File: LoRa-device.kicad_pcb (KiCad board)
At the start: 4 copper layers, 86.4 x 50.8 mm, 156 parts, among them J1 Micro_SD_Card_Det1, J3 Conn_01x04_Pin, J4 Conn_01x14_Pin, J6 Conn_01x04_Pin, J8 U.FL, P1 1_25T-1-2A, SW1 EVQPUC02K, SW2 EVQPUC02K, U1 ESP32-S3, U10 TPS2116DRL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

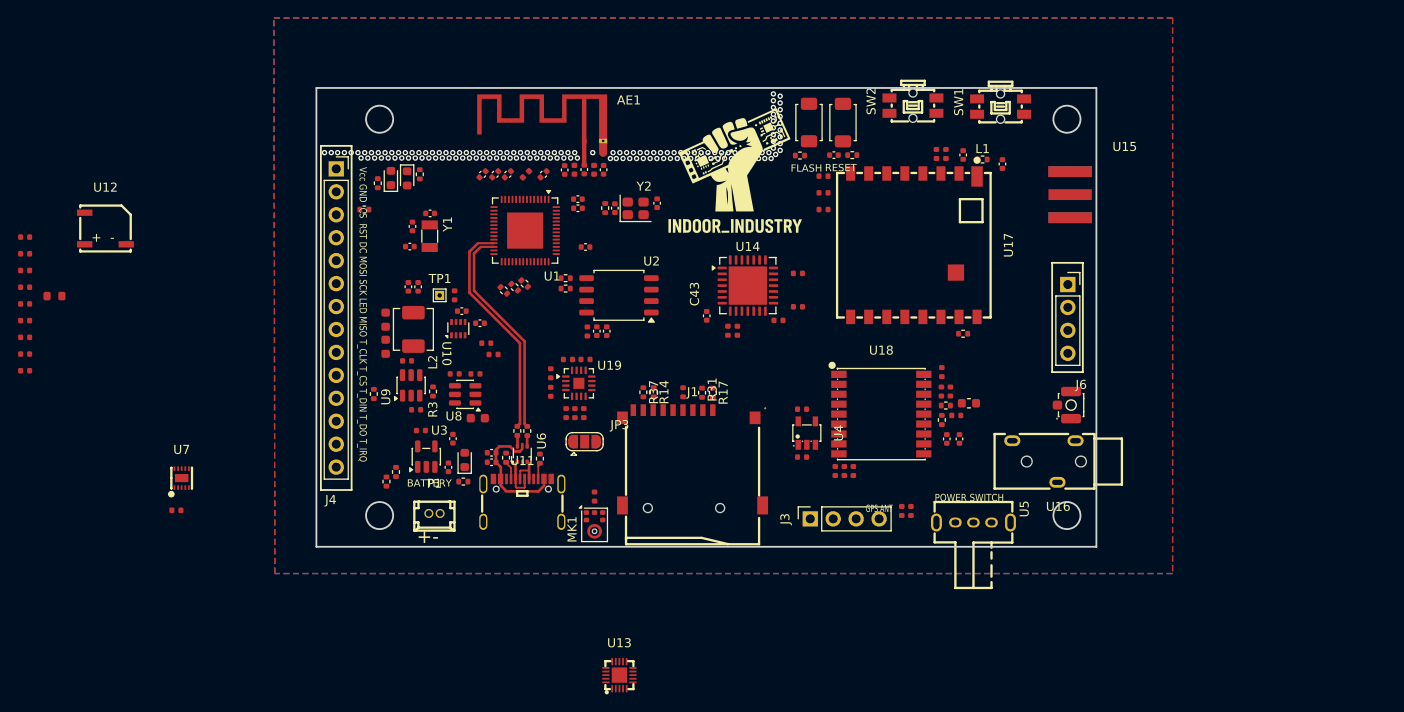
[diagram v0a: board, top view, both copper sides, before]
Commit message: Added buttons to case, rehauled power supply.
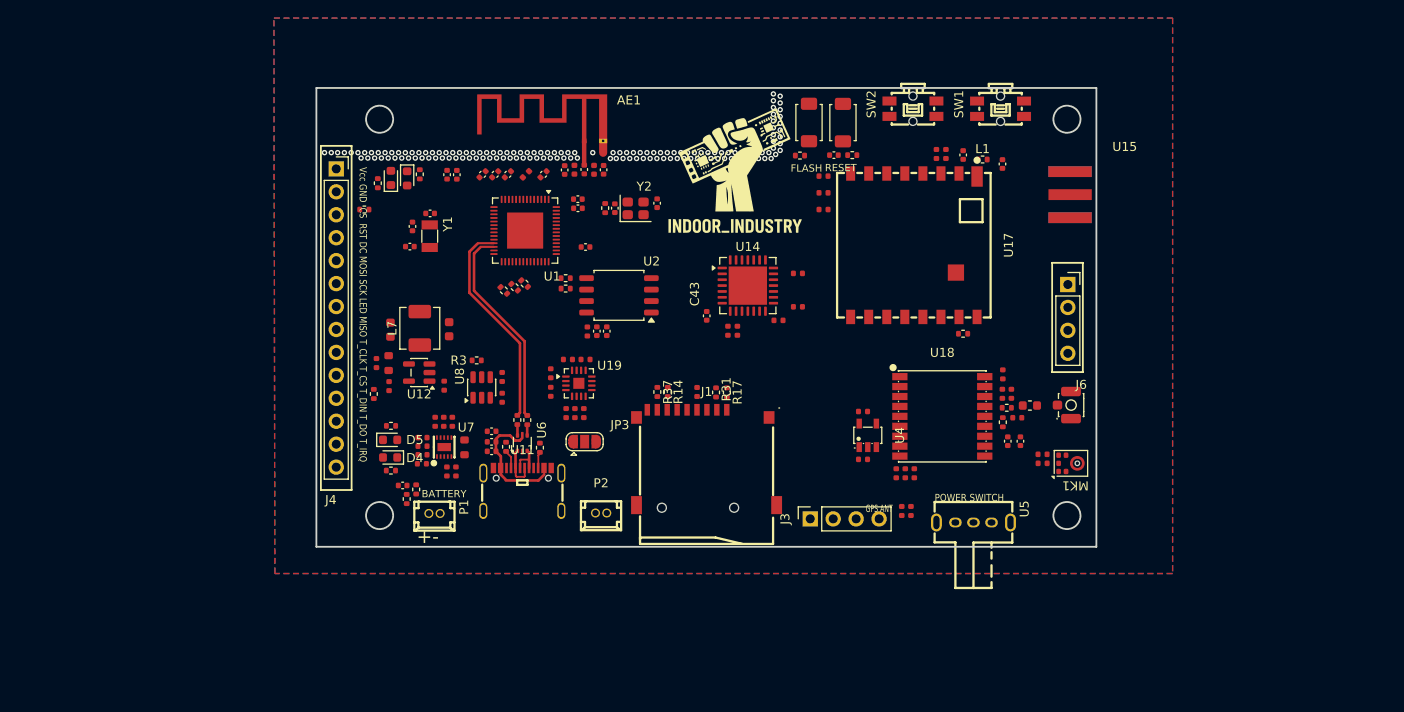
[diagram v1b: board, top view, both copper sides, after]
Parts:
- removed C1: 1uF, Capacitor_SMD:C_0402_1005Metric
- removed C12, C21, C50: 22uF, PCM_JLCPCB:C_0603
- removed C2: 10uF, Capacitor_SMD:C_0402_1005Metric
- removed C5: 10uF, PCM_JLCPCB:C_0402
- removed C9: 100nF, PCM_JLCPCB:C_0402
- removed D1: LED, LED_SMD:LED_0603_1608Metric
- removed L2: 4.7uH 3V, Inductor_SMD:L_Sunlord_MWSA0402S
- removed R15: 1K, Resistor_SMD:R_0402_1005Metric
- removed R20: 4.7kΩ, PCM_JLCPCB:R_0402
- removed R32: 100kΩ, PCM_JLCPCB:R_0402
- removed R33: 8.2kΩ, PCM_JLCPCB:R_0402
- removed R6: 22kΩ, PCM_JLCPCB:R_0402
- removed TP1: TestPoint, TestPoint:TestPoint_THTPad_1.0x1.0mm_Drill0.5mm
- removed U10: TPS2116DRL, Package_TO_SOT_SMD:SOT-583-8
- removed U13: ES8311, LoRa_library:WQFN-20_L3.0-W3.0-P0.40-BL-EP1.7
- removed U16: Black_headphone_jack, LoRa_library:AUDIO-TH_320B
- removed U3: TP4055, Package_TO_SOT_SMD:SOT-23-5
- removed U9: AP63203WU, Package_TO_SOT_SMD:TSOT-23-6
- added C54: 4.7uF, PCM_JLCPCB:C_0402, F.Cu at (116.0, 106.8)
- added C55: 10uF, PCM_JLCPCB:C_0603, F.Cu at (116.6, 100.5)
- added C56: 22uF, PCM_JLCPCB:C_0603, F.Cu at (110.1, 100.6)
- added C57: 6.8pF, PCM_JLCPCB:C_0402, F.Cu at (108.5, 104.3)
- added D4: LED, LED_SMD:LED_0603_1608Metric, F.Cu at (110.1, 114.8)
- added D5: LED, LED_SMD:LED_0603_1608Metric, F.Cu at (110.1, 112.8)
- added L7: 4.7uH 3V, Inductor_SMD:L_Sunlord_MWSA0402S, F.Cu at (113.3, 100.5)
- added P2: 1_25T-1-2A, LoRa_library:CONN-TH_1.25T-1-2A, F.Cu at (133.4, 120.9)
- added R54: 1K, Resistor_SMD:R_0402_1005Metric, F.Cu at (110.2, 116.2)
- added R55: 1K, Resistor_SMD:R_0402_1005Metric, F.Cu at (110.2, 111.2)
- added R56: 150kΩ, PCM_JLCPCB:R_0402, F.Cu at (110.0, 106.8)
- added R57: 680kΩ, PCM_JLCPCB:R_0603, F.Cu at (109.9, 104.3)
- U12: value MLT-5020 -> TLV62569DBV; footprint LoRa_library:BUZ-SMD_L5.0-W5.5-P4.60 -> Package_TO_SOT_SMD:SOT-23-5
- moved R1 96.1 mm to (182.3, 114.4), turned to 180 degrees
- moved MK1 53.2 mm to (185.4, 115.4), turned to 90 degrees
- moved R41 51.2 mm to (117.4, 116.3), turned to -90 degrees
- moved R43 49.7 mm to (182.3, 115.4), turned to 180 degrees
- moved C42 49.7 mm to (113.7, 113.5), turned to 180 degrees
- moved R49 48.6 mm to (117.0, 110.8), turned to 90 degrees
- moved C52 48.5 mm to (113.7, 114.4), turned to 180 degrees
- moved C51 48.5 mm to (113.7, 112.5), turned to 180 degrees
- moved R52 48.5 mm to (116.4, 116.3), turned to 90 degrees
- moved R51 48.4 mm to (118.3, 113.6), turned to -90 degrees
- moved C53 48.1 mm to (113.6, 115.4), turned to 180 degrees
- moved R50 47.3 mm to (116.0, 110.8), turned to 90 degrees
- moved R53 45.8 mm to (115.1, 110.8), turned to -90 degrees
- moved U12 38.2 mm to (113.3, 105.3), turned to 180 degrees
- moved U7 29.3 mm to (116.0, 113.6)
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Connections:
- R52 pad 2: Net-(U7-STAT2) -> GPB5
- R53 pad 2: Net-(U7-STAT1) -> GPA1
- U12 pad 1: unconnected-(U12-+-Pad1) -> VSYS_SW
- U12 pad 2: unconnected-(U12---Pad2) -> GND
- U12 pad 3: unconnected-(U12-NC-Pad3) -> Net-(U12-SW)
- U14 pad 18: unconnected-(U14-GPA1-Pad18) -> GPA1
- U14 pad 2: unconnected-(U14-GPB5-Pad2) -> GPB5
- U7 pad 3: Net-(U7-STAT2) -> GPB5
- U7 pad 9: Net-(U7-STAT1) -> GPA1
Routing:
- net USB_D+: track 24.0 -> 22.8 mm
- net USB_D-: track 24.8 -> 23.6 mm

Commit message: Almost ready for routing, major fixes, case ready.
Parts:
- removed C34: 1uF, PCM_JLCPCB:C_0402
- removed C51: 2.2uF, PCM_JLCPCB:C_0402
- removed C52: 10uF, PCM_JLCPCB:C_0402
- removed R57: 680kΩ, PCM_JLCPCB:R_0603
- added C1: 2.2uF, PCM_JLCPCB:C_0603, F.Cu at (113.7, 111.3)
- added C2: 10uF, PCM_JLCPCB:C_0603, F.Cu at (116.0, 116.8)
- added C5: 4.7uF, PCM_JLCPCB:C_0402, F.Cu at (162.5, 108.6)
- added C9: 100nF, PCM_JLCPCB:C_0402, F.Cu at (162.5, 109.7)
- added R32: 510Ω, PCM_JLCPCB:R_0402, F.Cu at (116.0, 110.8)
- added R33: 100kΩ, PCM_JLCPCB:R_0402, F.Cu at (112.8, 108.5)
- R50: value 330Ω -> 300kΩ; footprint PCM_JLCPCB:R_0402 -> PCM_JLCPCB:R_0603
- R56: footprint PCM_JLCPCB:R_0402 -> PCM_JLCPCB:R_0603
- moved R50 5.50 mm to (110.8, 109.2), turned to 180 degrees
- moved C36 3.07 mm to (174.1, 83.0)
- moved DNP2 3.07 mm to (176.0, 83.1)
- moved L1 3.07 mm to (178.1, 83.6)
- moved R10 3.07 mm to (175.9, 102.9)
- moved R44 3.07 mm to (160.5, 89.2)
- moved R46 3.07 mm to (160.5, 85.5)
- moved C7 3.07 mm to (173.0, 83.0)
- moved DNP4 3.07 mm to (180.3, 84.1)
- moved R45 3.07 mm to (160.5, 87.3)
- moved U17 3.07 mm to (170.5, 93.1)
- moved R56 1.13 mm to (110.8, 107.7), turned to 0 degrees
- moved R41 0.85 mm to (118.2, 116.3)
- moved R52 0.85 mm to (117.2, 116.3)
- moved C44 0.81 mm to (166.7, 121.5)
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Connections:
- D3 pad 2: GPA5 -> GPA7
- R50 pad 1: Net-(U7-ISET) -> VDD_CPU
- R50 pad 2: GND -> Net-(R50-Pad2)
- R56 pad 1: Net-(U12-FB) -> Net-(R50-Pad2)
- R56 pad 2: GND -> Net-(U12-FB)
- SW1 pad 3: GPA7 -> GPA5
- SW2 pad 3: GPB7 -> GPB2
- U14 pad 27: LORA_RF_EN -> GPB2
- U14 pad 4: GPB7 -> LORA_RF_EN
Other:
- outline, holes or cut-outs redrawn
- board text added: "AUDIO OUT"

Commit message: Case prototype ready. Added thermal pads.
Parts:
- removed C57: 6.8pF, PCM_JLCPCB:C_0402
- removed R24, R42: 330Ω, PCM_JLCPCB:R_0402
- added R15: 33Ω, PCM_JLCPCB:R_0402, F.Cu at (158.9, 118.8)
- added R20: 33Ω, PCM_JLCPCB:R_0402, F.Cu at (156.5, 118.8)
- added R6: 330Ω, PCM_JLCPCB:R_0402, F.Cu at (130.8, 91.9)
- moved DNP1 4.25 mm to (127.5, 86.7), turned to -45 degrees
- moved C14 3.83 mm to (132.9, 86.7), turned to -45 degrees
- moved R30 3.62 mm to (125.0, 99.0)
- moved L6 3.21 mm to (128.3, 85.2), turned to 45 degrees
- moved R29 3.06 mm to (125.8, 98.3)
- moved L5 2.61 mm to (131.5, 85.2), turned to 135 degrees
- moved C39 2.60 mm to (129.4, 89.3)
- moved C40 2.60 mm to (129.3, 88.3)
- moved R28 2.56 mm to (126.5, 97.5)
- moved C33 2.29 mm to (138.8, 88.7)
- moved R23 2.29 mm to (133.0, 89.3)
- moved Y2 2.29 mm to (136.4, 89.3)
- moved C38 2.29 mm to (111.7, 91.3)
- moved U1 2.29 mm to (124.2, 91.8)
- moved Y1 2.29 mm to (113.6, 92.4)
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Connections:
- J3 pad 1: MTDO/IO40/I2C_SCK -> Net-(J3-Pin_1)
- J3 pad 2: MTMS/IO42/I2C_SDA -> Net-(J3-Pin_2)
- R47 pad 2: MTMS/IO42/I2C_SDA -> Net-(J3-Pin_2)
- R48 pad 2: MTDO/IO40/I2C_SCK -> Net-(J3-Pin_1)
- U1 pad 45: Net-(U1-MTDO) -> MTDO/IO40/I2C_SCK
- U1 pad 48: Net-(U1-MTMS) -> MTMS/IO42/I2C_SDA
- U1 pad 49: GPS_RXD -> Net-(U1-U0TXD)
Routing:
- net Net-(AE1-FEED): track 2.63 -> 8.26 mm
- net Net-(U1-LNA_IN): track 0.00 -> 3.30 mm
- net USB_D-: track 23.6 -> 22.9 mm
- net USB_D+: track 22.8 -> 22.2 mm
- added copper zone on In2.Cu, net GND
- removed copper zone on In2.Cu, net VDD_CPU

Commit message: Ready for routing!
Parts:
- removed DNP1: ~, Capacitor_SMD:C_0402_1005Metric
- removed L4: 68nH,300mA, PCM_JLCPCB:L_0603
- added C12: 1.4pF, Capacitor_SMD:C_0402_1005Metric, F.Cu at (126.7, 85.9)
- added JP1: Jumper_2_Open, Jumper:SolderJumper-2_P1.3mm_Open_RoundedPad1.0x1.5mm, F.Cu at (109.5, 95.8)
- added L2: 68nH, Inductor_SMD:L_0402_1005Metric, F.Cu at (182.2, 107.8)
- C31: value 15pF -> 1.4pF
- L6: value 4.7nH -> 2.7nH
- moved J4 33.0 mm to (103.9, 115.8), turned to 180 degrees
- moved R44 7.63 mm to (165.4, 83.3)
- moved R45 4.94 mm to (163.4, 83.3)
- moved G*** 4.79 mm to (147.1, 89.0)
- moved R47 4.05 mm to (151.1, 103.8)
- moved U14 4.05 mm to (152.3, 98.8)
- moved C43 4.05 mm to (147.7, 102.2)
- moved R4 4.05 mm to (155.7, 102.7)
- moved R48 4.05 mm to (150.1, 103.8)
- moved DNP2 2.82 mm to (178.3, 84.6)
- moved C27 2.70 mm to (182.1, 111.2)
- moved L1 2.38 mm to (180.0, 85.0)
- moved DNP7 2.33 mm to (180.6, 110.7), turned to 90 degrees
- moved R46 2.29 mm to (161.3, 83.3)
- moved DNP4 1.93 mm to (181.7, 85.5)
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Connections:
- J1 pad 3: MOSIA -> MOSIB
- J1 pad 5: SCKA -> SCKB
- J1 pad 7: MISOA -> MISOB
- J4 pad 10: SCKB -> SCKA
- J4 pad 12: MOSIB -> MOSIA
- J4 pad 13: MISOB -> MISOA
- J4 pad 9: MISOB -> Net-(J4-Pin_9)
- R14 pad 2: MISOA -> MISOB
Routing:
- net USB_D-: track 22.9 -> 0.00 mm
- net USB_D+: track 22.2 -> 0.00 mm
- net +5V: track 13.5 -> 0.31 mm
- net Net-(AE1-FEED): track 8.26 -> 0.00 mm
- net Net-(U11-DP1): track 4.87 -> 0.00 mm
- net Net-(U11-DN1): track 4.87 -> 0.00 mm
- net Net-(U1-LNA_IN): track 3.30 -> 0.08 mm
- net Net-(U11-CC1): track 1.93 -> 0.00 mm
- net Net-(U11-CC2): track 1.76 -> 0.00 mm
- net Net-(R2-Pad1): track 1.20 -> 0.00 mm
- net Net-(R18-Pad1): track 1.19 -> 0.00 mm
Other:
- board text added: "SCK SDA GND 3V3"
- board text added: "T_IRQ T_DO T_DIN T_CS T_CLK MISO LED SCK MOSI DC RST CS GND VCC"
- board text removed: "Vcc GND CS RST DC MOSI SCK LED MISO T_CLK T_CS T_DIN T_DO T_IRQ"

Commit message: Minor layout changes
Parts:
- moved R13 22.7 mm to (108.1, 110.0), turned to -90 degrees
- moved R11 17.3 mm to (108.2, 90.4)
- moved R30 5.74 mm to (129.6, 96.0)
- moved C33 5.74 mm to (143.4, 85.6)
- moved C39 5.74 mm to (134.0, 86.2)
- moved C49 5.74 mm to (138.0, 98.6)
- moved R23 5.74 mm to (137.7, 86.2)
- moved R26 5.74 mm to (135.6, 92.7)
- moved R27 5.74 mm to (135.6, 93.8)
- moved R6 5.74 mm to (135.5, 88.8)
- moved U2 5.74 mm to (141.5, 94.6)
- moved Y1 5.74 mm to (118.3, 89.3)
- moved Y2 5.74 mm to (141.1, 86.2)
- moved C10 5.74 mm to (118.3, 86.8)
- moved C37 5.74 mm to (116.1, 90.4)
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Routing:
- net GND: track 1.32 -> 0.00 mm, vias 140 -> 142

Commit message: Routing started
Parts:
- removed JP1: Jumper_2_Open, Jumper:SolderJumper-2_P1.3mm_Open_RoundedPad1.0x1.5mm
- added H1: MountingHole, MountingHole:MountingHole_3mm, F.Cu at (184.9, 121.3)
- added H2: MountingHole, MountingHole:MountingHole_3mm, F.Cu at (108.9, 77.3)
- added H3: MountingHole, MountingHole:MountingHole_3mm, F.Cu at (184.9, 77.3)
- added H4: MountingHole, MountingHole:MountingHole_3mm, F.Cu at (108.9, 121.3)
- added R24: 0R, Resistor_SMD:R_0402_1005Metric, F.Cu at (108.3, 91.6)
- moved G*** 64.4 mm to (212.9, 97.0)
- moved D2 33.3 mm to (142.7, 91.0)
- moved R25 33.3 mm to (145.9, 90.6)
- moved D3 33.3 mm to (144.5, 91.1)
- moved R16 33.3 mm to (141.3, 91.6)
- moved R39 18.2 mm to (123.8, 83.8)
- moved R40 18.2 mm to (121.9, 83.8)
- moved R47 14.9 mm to (160.1, 117.3), turned to -90 degrees
- moved R48 14.3 mm to (157.6, 117.4), turned to -90 degrees
- moved C32 11.3 mm to (129.3, 101.5), turned to 180 degrees
- moved U2 11.3 mm to (133.3, 102.2), turned to 90 degrees
- moved R41 10.5 mm to (110.9, 108.8), turned to 90 degrees
- moved C13 9.94 mm to (129.3, 100.4), turned to 180 degrees
- moved R38 9.58 mm to (130.6, 113.0)
- moved D4 9.53 mm to (104.0, 122.1)
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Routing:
- net VDD_CPU: track 0.00 -> 252.8 mm, vias 0 -> 36
- net MOSIB: track 0.00 -> 66.4 mm, vias 0 -> 2
- net Net-(U8-~{ON}): track 0.00 -> 62.3 mm, vias 0 -> 1
- net SCKB: track 0.00 -> 61.6 mm, vias 0 -> 2
- net MISOB: track 0.00 -> 51.9 mm, vias 0 -> 2
- net TOUCH_IRQ: track 0.00 -> 49.2 mm, vias 0 -> 1
- net MOSIA: track 0.00 -> 47.6 mm, vias 0 -> 2
- net GPS_TXD: track 0.00 -> 41.7 mm
- net SCKA: track 0.00 -> 41.5 mm, vias 0 -> 2
- net GPS_RXD: track 0.00 -> 39.9 mm
- net GPA5: track 0.00 -> 36.6 mm, vias 0 -> 2
- net EN: track 0.00 -> 35.0 mm, vias 0 -> 2
- net GPB2: track 0.00 -> 31.8 mm, vias 0 -> 2
- net IO0: track 0.00 -> 30.9 mm, vias 0 -> 2
- net SCREEN_LED: track 0.00 -> 29.0 mm, vias 0 -> 1
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- added copper zone on F.Cu, net VDD_CPU
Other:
- outline, holes or cut-outs redrawn

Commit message: More routing, modifying case buttons and locking
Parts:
- moved G*** 61.3 mm to (152.3, 87.5)
- moved D2 24.1 mm to (119.4, 97.2)
- moved R16 24.1 mm to (118.0, 97.7), turned to -90 degrees
- moved R6 6.15 mm to (137.8, 93.8), turned to -45 degrees
- moved D3 3.92 mm to (140.7, 92.0)
- moved R25 3.92 mm to (142.1, 91.5)
- moved C1 2.84 mm to (117.3, 112.4)
- moved C2 2.60 mm to (117.5, 108.9), turned to 90 degrees
- moved Y1 2.16 mm to (116.5, 89.6)
- moved C37 2.16 mm to (114.7, 90.7)
- moved C38 2.16 mm to (114.7, 88.5)
- moved C42 1.88 mm to (116.8, 113.5), turned to 0 degrees
- moved C11 1.54 mm to (135.4, 91.6), turned to -45 degrees
- moved R20 1.41 mm to (155.1, 117.3)
- moved R48 1.41 mm to (156.2, 117.3)
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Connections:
- D3 pad 2: GPA7 -> GPB7
- J1 pad 2: SD_CS -> SPICLK_N/IO48/SD_CS
- R10 pad 2: SPICLK_N/IO48/LORA_CS -> LORA_CS
- R31 pad 2: SD_CS -> SPICLK_N/IO48/SD_CS
- U1 pad 10: SCREEN_DC -> LORA_IO1
- U1 pad 23: SD_CS -> SCREEN_DC
- U1 pad 24: LORA_IO1 -> SCREEN_CS
- U1 pad 36: SPICLK_N/IO48/LORA_CS -> SPICLK_N/IO48/SD_CS
- U1 pad 7: SCREEN_CS -> LORA_CS
- U14 pad 17: LORA_RST -> GPS_WKUP
- U14 pad 21: GPS_WKUP -> LORA_RST
- U14 pad 24: GPA7 -> LORA_RF_EN
- U14 pad 25: LORA_IO2 -> LORA_IO3
- U14 pad 26: LORA_IO3 -> LORA_IO2
- U14 pad 4: LORA_RF_EN -> GPB7
- U17 pad 15: SPICLK_N/IO48/LORA_CS -> LORA_CS
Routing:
- net VDD_CPU: track 252.8 -> 380.3 mm, vias 36 -> 46
- net IO8: track 0.00 -> 80.1 mm, vias 0 -> 2
- net MISOA: track 0.00 -> 78.8 mm, vias 0 -> 3
- net GPA1: track 1.69 -> 80.1 mm, vias 0 -> 2
- net SCREEN_RST: track 0.00 -> 67.8 mm, vias 0 -> 1
- net GPB5: track 7.84 -> 70.7 mm, vias 2 -> 4
- net LORA_CS: track 0.00 -> 59.6 mm, vias 0 -> 2
- net VBAT: track 10.3 -> 69.2 mm, vias 0 -> 5
- net IO4: track 0.00 -> 58.4 mm, vias 0 -> 2
- net IO1: track 0.00 -> 56.2 mm, vias 0 -> 2
- net GPA6: track 0.00 -> 53.1 mm, vias 0 -> 2
- net LORA_BUSY: track 0.00 -> 49.0 mm, vias 0 -> 2
- net LORA_IO1: track 0.00 -> 41.3 mm, vias 0 -> 2
- net IO10: track 0.00 -> 40.4 mm, vias 0 -> 2
- net SCKA: track 41.5 -> 81.2 mm, vias 2 -> 4
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- added copper zone on F.Cu, net VBAT
- added copper zone on In2.Cu, net VDD_CPU

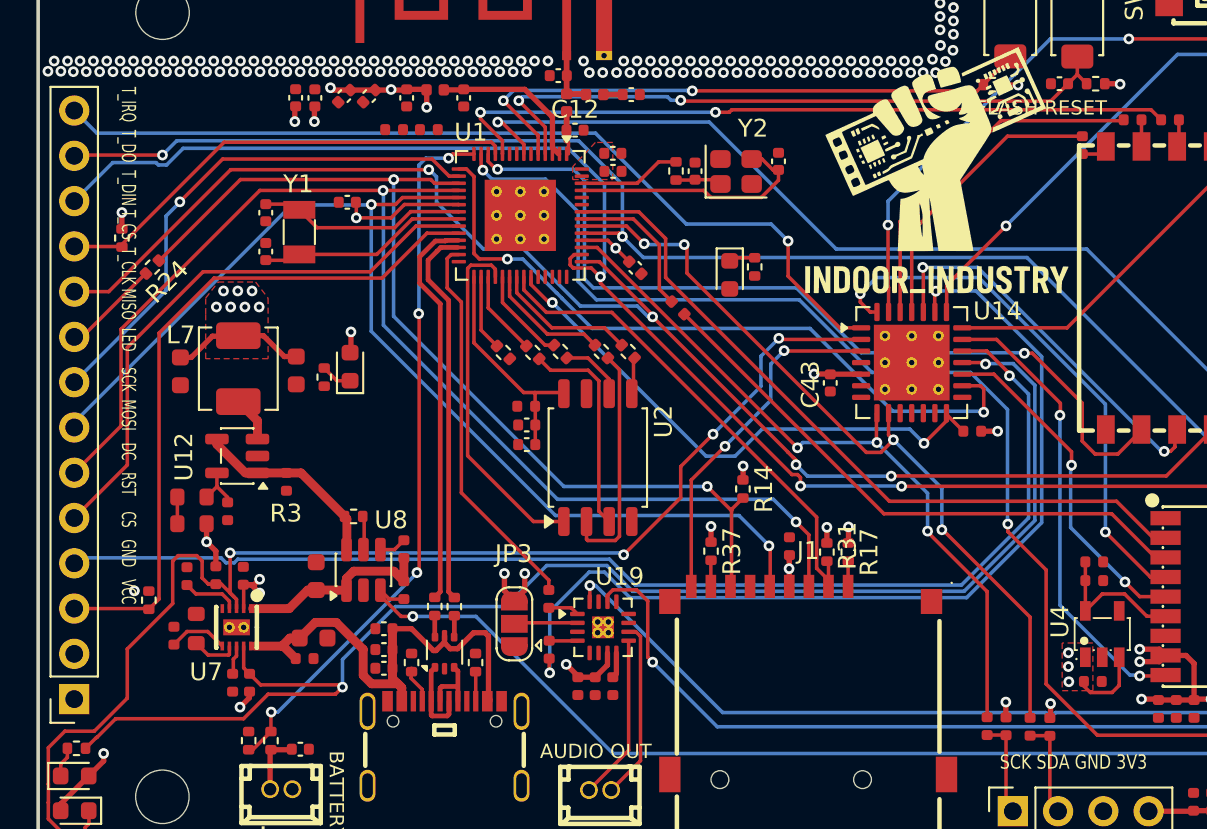
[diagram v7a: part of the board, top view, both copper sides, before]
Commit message: Modified case and progressed routing
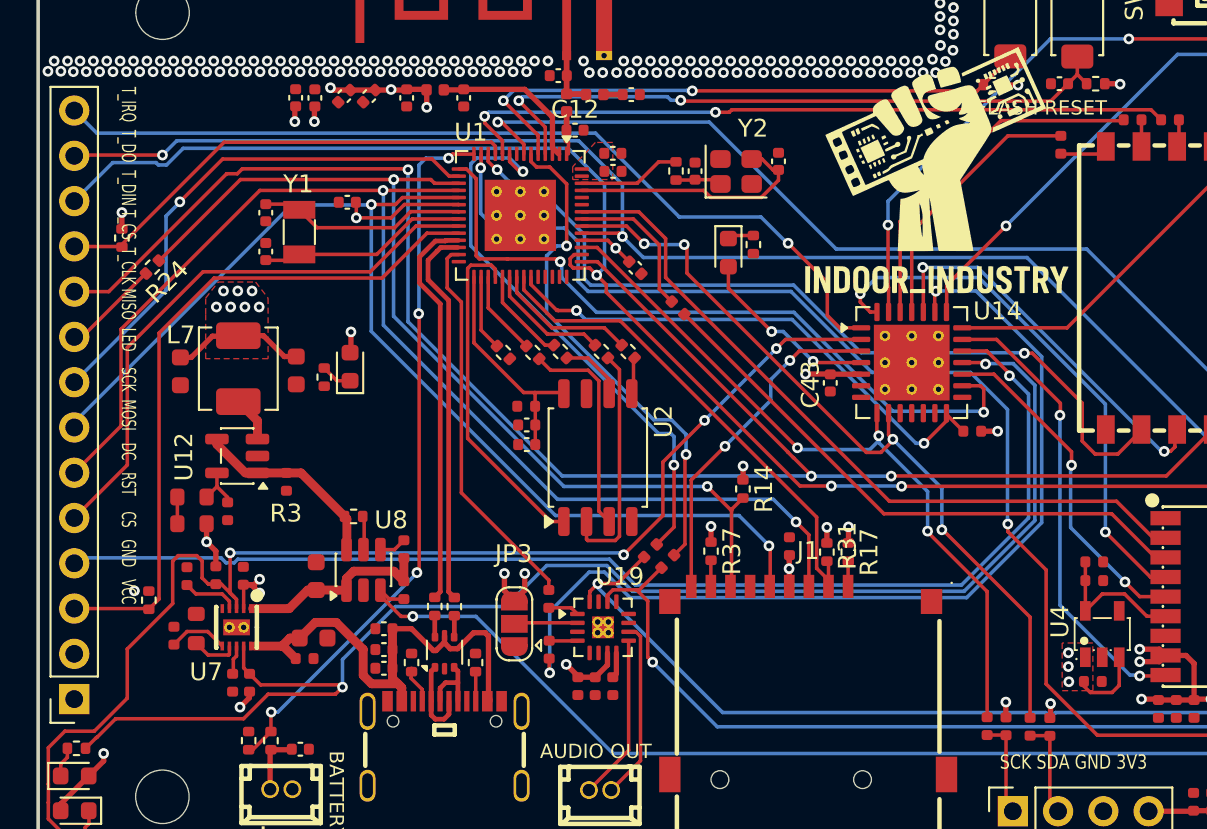
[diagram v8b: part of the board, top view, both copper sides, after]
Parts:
- moved R39 27.7 mm to (137.2, 108.1), turned to 45 degrees
- moved R40 27.7 mm to (136.2, 107.5), turned to 45 degrees
- moved D3 1.25 mm to (140.6, 90.8)
- moved R25 1.25 mm to (142.0, 90.3)
- moved R46 1.21 mm to (159.3, 84.7)
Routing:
- net Net-(U1-GPIO4): track 0.00 -> 31.7 mm, vias 0 -> 2
- net Net-(U1-GPIO1): track 0.00 -> 28.7 mm, vias 0 -> 2
- net SCKA: track 81.2 -> 97.8 mm, vias 4 -> 3
- net GPB7: track 0.00 -> 10.4 mm, vias 0 -> 2
- net IO4: track 58.4 -> 61.7 mm
- net IO1: track 56.2 -> 58.1 mm
- net LORA_BUSY: track 49.0 -> 47.7 mm
- net SPICLK_P/IO47/EXP_RST: track 31.0 -> 29.8 mm
- net Net-(U17-DIO3): track 1.50 -> 2.71 mm
- net LORA_IO3: track 16.3 -> 15.1 mm
- net SPICS0: track 19.6 -> 19.0 mm
- net GPB6: track 19.7 -> 19.2 mm
- net IO8: track 80.1 -> 80.6 mm
